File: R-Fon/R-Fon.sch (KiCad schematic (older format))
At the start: 23 parts, among them P1 BatteryConnector, P2 Speaker Connector, Q1 BC546, Q2 BC546, Q3 BC546, SW1 ON/OFF Switch, SW2 SOUND ON/OFF

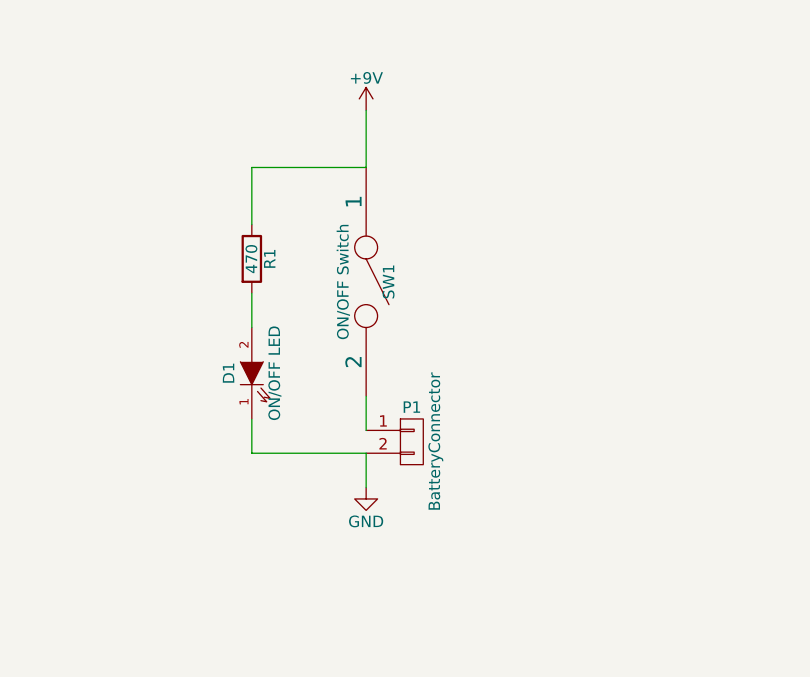
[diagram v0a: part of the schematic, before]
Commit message: changed battery switch design.
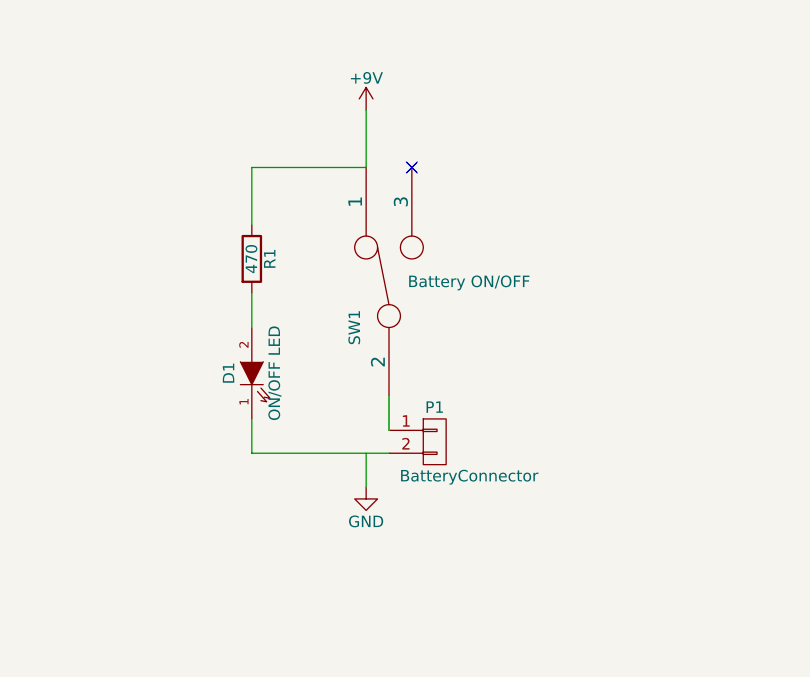
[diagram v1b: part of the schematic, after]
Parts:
- removed SW1: ON/OFF Switch, symbol SPST
- added SW1: Battery ON/OFF, symbol SWITCH_INV
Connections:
- net +9V: now also SW1.1
- net GND: no longer D1.1 (K), P1.2 (P2)
- net at P1.1 (P1): now also SW1.2
- new net: D1.1 (K), P1.2 (P2)
- no-connect marks 0 -> 1
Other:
- moved on the sheet: P1
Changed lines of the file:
@@
 	0    -1   -1   0
 $EndComp
-$Comp
-L SPST SW1
-U 1 1 59216F8B
-P 3050 6100
-F 0 "SW1" H 3050 6200 50  0000 C CNN
-F 1 "ON/OFF Switch" H 3050 6000 50  0000 C CNN
-F 2 "" H 3050 6100 60  0000 C CNN
-F 3 "" H 3050 6100 60  0000 C CNN
-	1    3050 6100
-	0    1    1    0
-$EndComp
 Wire Wire Line
 	3050 6850 3050 7000
-Wire Wire Line
-	3050 6750 3050 6600
 $Comp
 L BC546 Q3
@@
 Wire Wire Line
 	2550 6700 2550 6850
-Wire Wire Line
-	2550 6850 3050 6850
 $Comp
 L BatteryConnector P1
 U 1 1 5921CB81
-P 3250 6800
-F 0 "P1" H 3250 6950 50  0000 C CNN
-F 1 "BatteryConnector" V 3350 6800 50  0000 C CNN
-F 2 "" H 3250 6800 60  0000 C CNN
-F 3 "" H 3250 6800 60  0000 C CNN
-	1    3250 6800
+P 3350 6800
+F 0 "P1" H 3350 6950 50  0000 C CNN
+F 1 "BatteryConnector" H 3500 6650 50  0000 C CNN
+F 2 "" H 3350 6800 60  0000 C CNN
+F 3 "" H 3350 6800 60  0000 C CNN
+	1    3350 6800
 	1    0    0    -1
 $EndComp
@@
 Text Notes 6250 4600 0    60   ~ 0
 Measurement terminals and overcurrent protection
+$Comp
+L SWITCH_INV SW1
+U 1 1 5921E019
+P 3150 6100
+F 0 "SW1" H 2950 6250 50  0000 C CNN
+F 1 "Battery ON/OFF" V 3150 5750 50  0000 C CNN
+F 2 "" H 3150 6100 60  0000 C CNN
+F 3 "" H 3150 6100 60  0000 C CNN
+	1    3150 6100
+	0    -1   -1   0
+$EndComp
+Wire Wire Line
+	2550 6850 3150 6850
+Wire Wire Line
+	3150 6600 3150 6750
+NoConn ~ 3250 5600
 $EndSCHEMATC

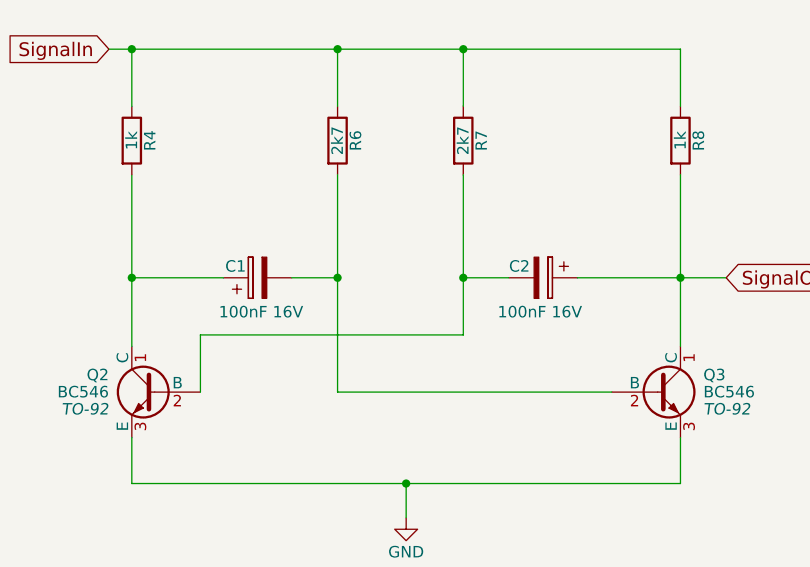
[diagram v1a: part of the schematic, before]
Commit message: changed C symbol
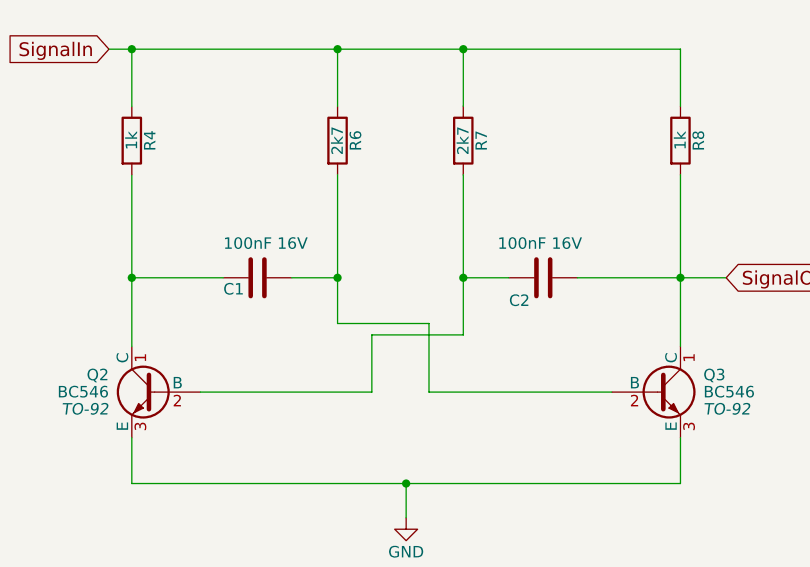
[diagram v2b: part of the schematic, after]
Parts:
- removed C1, C2: 100nF 16V, symbol CP
- added C1, C2: 100nF 16V, symbol C
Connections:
- net SignalOut: now also C2.1
- net at Q2.1 (C), R4.2: now also C1.2
- net at Q3.2 (B), R6.2: now also C1.1
- net at Q2.2 (B), R7.2: now also C2.2
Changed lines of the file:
@@
 $EndDescr
-$Comp
-L CP C1
-U 1 1 59216D2A
-P 2700 2300
-F 0 "C1" V 2750 2350 50  0000 L CNN
-F 1 "100nF 16V" V 2550 2100 50  0000 L CNN
-F 2 "" H 2738 2150 30  0000 C CNN
-F 3 "" H 2700 2300 60  0000 C CNN
-	1    2700 2300
-	0    -1   -1   0
-$EndComp
 $Comp
 L R R4
@@
 $EndComp
 $Comp
-L CP C2
-U 1 1 59217EC5
-P 3950 2300
-F 0 "C2" V 3900 2150 50  0000 L CNN
-F 1 "100nF 16V" V 4100 2100 50  0000 L CNN
-F 2 "" H 3988 2150 30  0000 C CNN
-F 3 "" H 3950 2300 60  0000 C CNN
-	1    3950 2300
-	0    1    1    0
-$EndComp
-$Comp
 L R R6
 U 1 1 59217F7B
@@
 	2850 2300 3050 2300
 Wire Wire Line
-	3050 1850 3050 2800
-Wire Wire Line
 	2150 1550 2150 1300
 Wire Wire Line
@@
 Wire Wire Line
 	4550 1850 4550 2600
-Wire Wire Line
-	3050 2800 4250 2800
 Connection ~ 3050 2300
-Wire Wire Line
-	2450 2800 2450 2550
-Wire Wire Line
-	2450 2550 3600 2550
 Connection ~ 3600 2300
 Text GLabel 4750 2300 2    60   Input ~ 0
@@
 	3150 6600 3150 6750
 NoConn ~ 3250 5600
+$Comp
+L C C2
+U 1 1 59270D65
+P 3950 2300
+F 0 "C2" V 4050 2150 50  0000 L CNN
+F 1 "100nF 16V" V 3800 2100 50  0000 L CNN
+F 2 "" H 3988 2150 30  0000 C CNN
+F 3 "" H 3950 2300 60  0000 C CNN
+	1    3950 2300
+	0    1    1    0
+$EndComp
+$Comp
+L C C1
+U 1 1 59270EBD
+P 2700 2300
+F 0 "C1" V 2750 2150 50  0000 L CNN
+F 1 "100nF 16V" V 2550 2150 50  0000 L CNN
+F 2 "" H 2738 2150 30  0000 C CNN
+F 3 "" H 2700 2300 60  0000 C CNN
+	1    2700 2300
+	0    1    1    0
+$EndComp
+Wire Wire Line
+	2450 2800 3200 2800
+Wire Wire Line
+	3200 2800 3200 2550
+Wire Wire Line
+	3200 2550 3600 2550
+Wire Wire Line
+	3050 1850 3050 2500
+Wire Wire Line
+	3050 2500 3450 2500
+Wire Wire Line
+	3450 2500 3450 2800
+Wire Wire Line
+	3450 2800 4250 2800
 $EndSCHEMATC

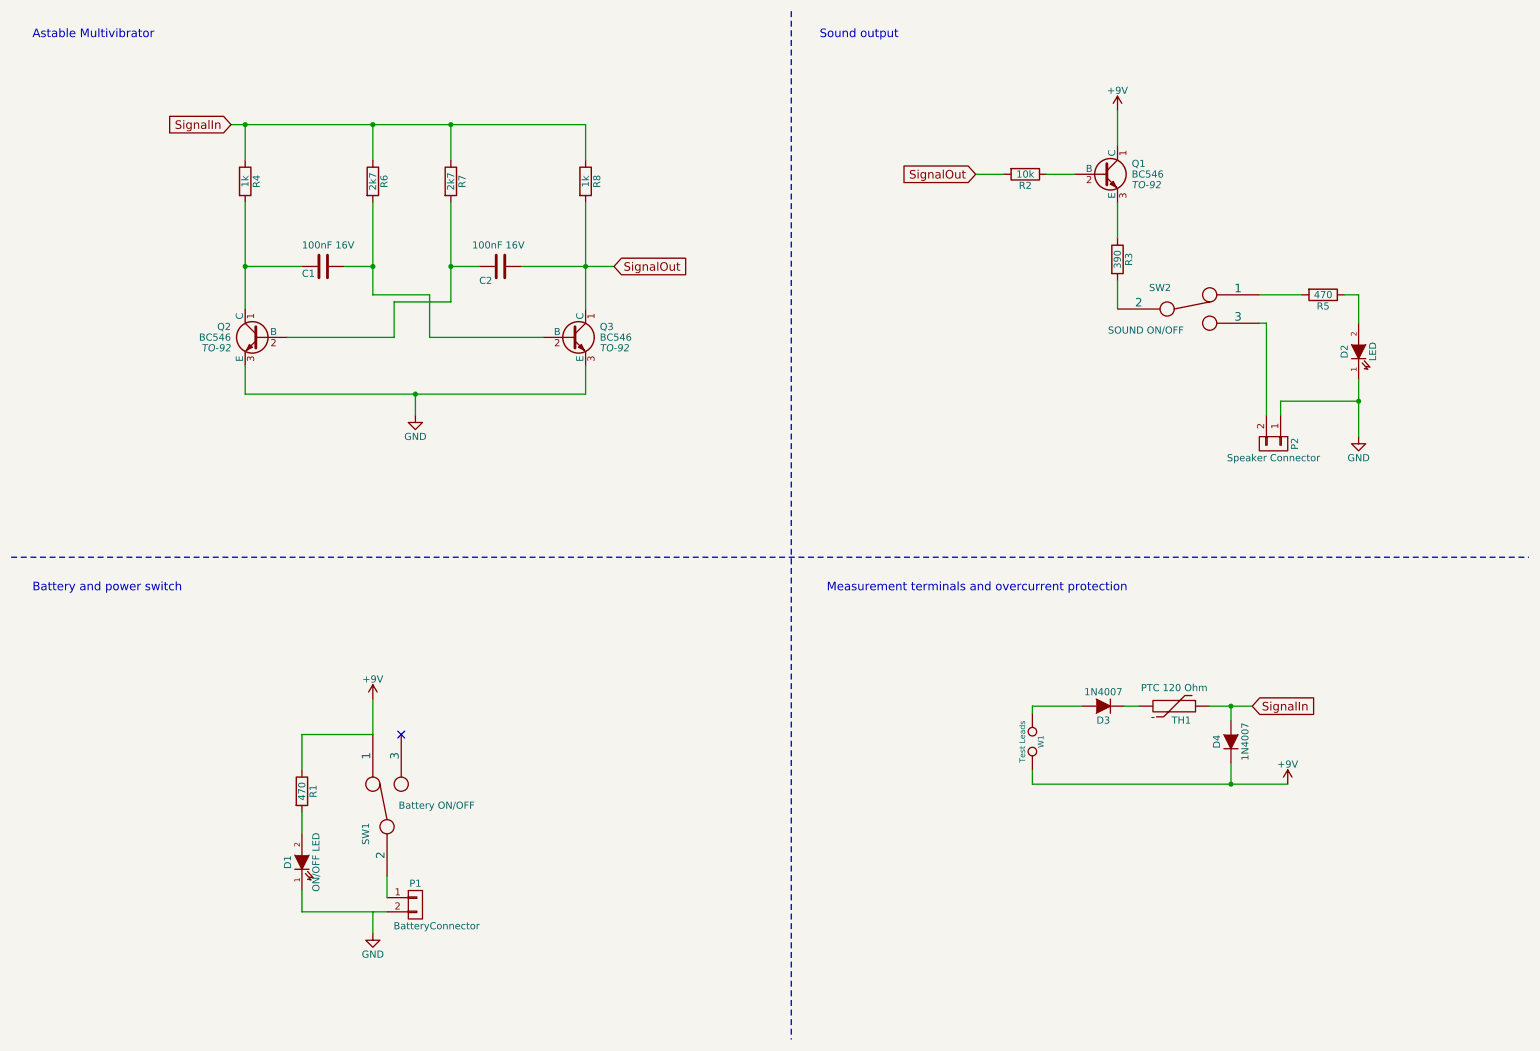
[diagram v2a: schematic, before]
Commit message: reflects first build
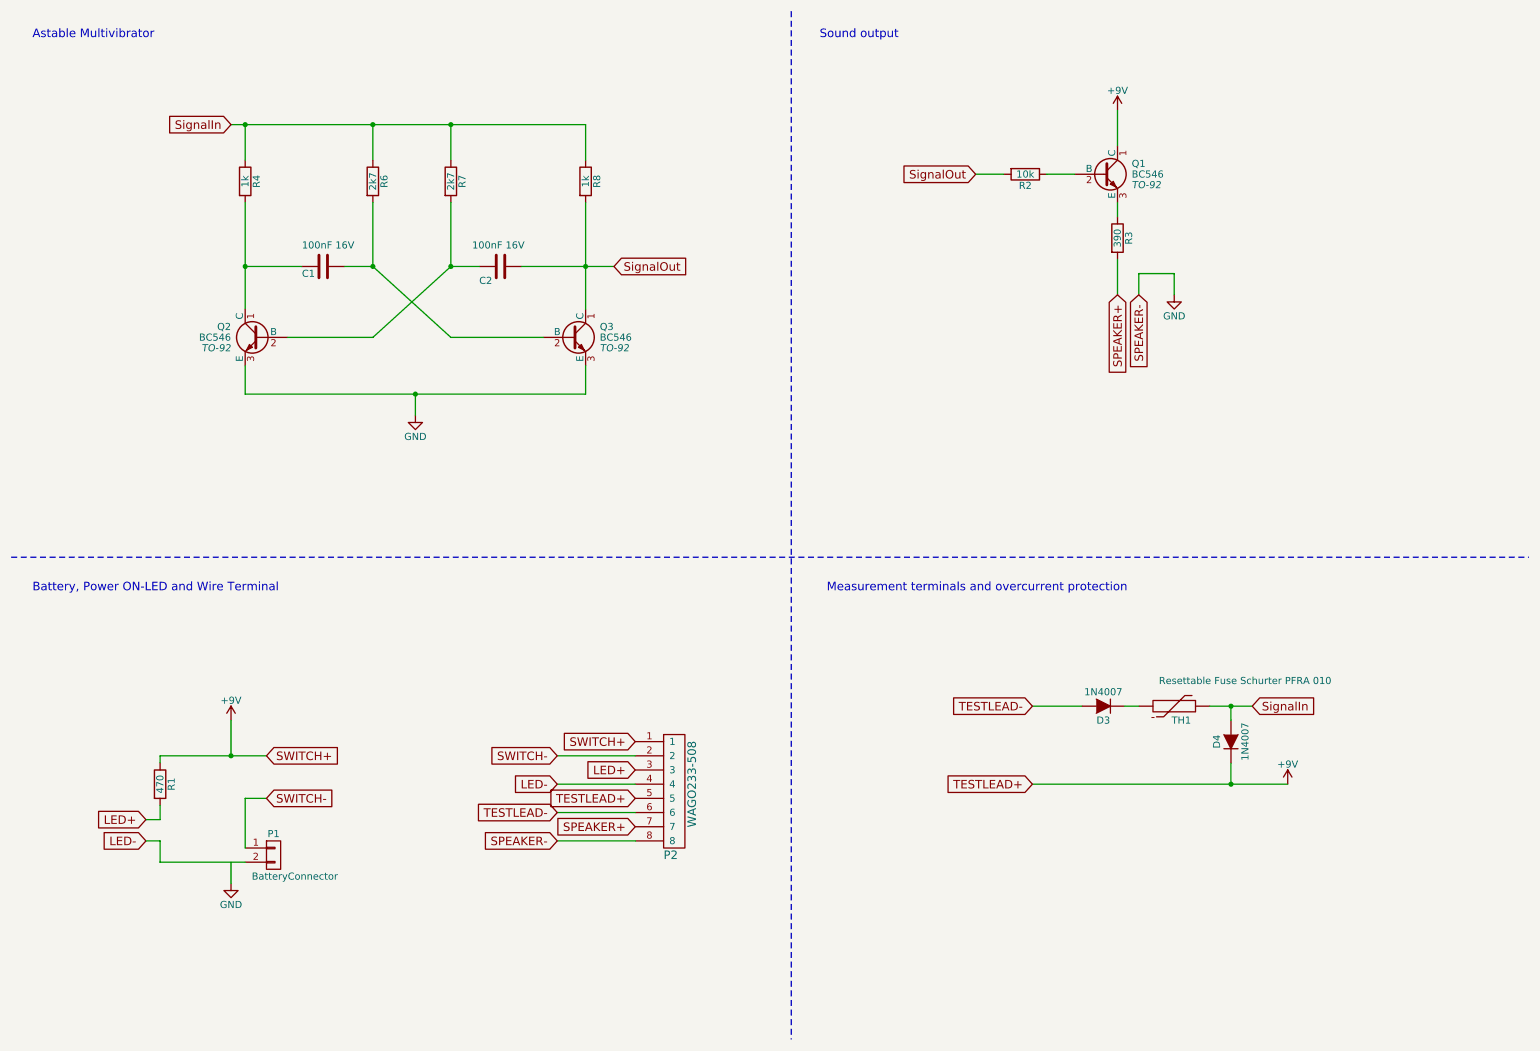
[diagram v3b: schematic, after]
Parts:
- removed D1: ON/OFF LED, symbol LED
- removed D2: LED, symbol LED
- removed P2: Speaker Connector, symbol CONN_01X02
- removed R5: 470, symbol R
- removed SW1: Battery ON/OFF, symbol SWITCH_INV
- removed SW2: SOUND ON/OFF, symbol SWITCH_INV
- removed W1: Test Leads, symbol TEST
- added P2: WAGO233-508, symbol WAGO233-508
- C1, C2: footprint (none) -> Capacitors_THT:C_Disc_D3.4mm_W2.1mm_P2.50mm
- D3, D4: footprint (none) -> Diodes_THT:Diode_DO-41_SOD81_Horizontal_RM10
- P1: footprint (none) -> Wire_Pads:SolderWirePad_2x_2-5mmDrill
- R1, R2, R3, R4, R6, R7, R8: footprint (none) -> Resistors_THT:Resistor_Horizontal_RM10mm
- TH1: value PTC 120 Ohm -> Resettable Fuse Schurter PFRA 010; footprint (none) -> Resistors_THT:R_Box_L8.4mm_W2.5mm_P5.08mm
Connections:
- net +9V: now also P2.1, P2.5
- net GND: now also P2.8
- net TESTLEAD-: now reaches D3.2 (A)
- net TESTLEAD-: now also P2.6
- net SPEAKER+: now reaches R3.2
- net SPEAKER+: now also P2.7
- net LED-: now reaches P1.2 (P2)
- net LED-: now also P2.4
- net LED+: now reaches R1.2
- net LED+: now also P2.3
- net SWITCH-: now reaches P1.1 (P1)
- net SWITCH-: now also P2.2
- no-connect marks 1 -> 0
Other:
- note added: "Battery, Power ON-LED and Wire Terminal"
- note removed: "Battery and power switch"
- moved on the sheet: P1, R1, R3
